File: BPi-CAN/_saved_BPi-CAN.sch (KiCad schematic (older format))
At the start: 82 parts, among them J1 RJ45, J2 RJ45, J3 RJ45, J4 RJ45, P1 BPi, P10 SPI, P11 SNIFFER, P12 CAN-Bus, P13 USB, P14 CAN-Bus, P15 POWER, P16 CAN, P17 CAN, P18 CAN, P19 TERM, P2 S88, P20 S88 CONN, P21 RS232 Con, P22 S88, P3 CONN_02X04, P4 CONN_01X02, P5 TERM, P6 S88, P7 I2C-Bus, P8 RS485, P9 RS232, U1 MCP2562, U10 MCP2562, U11 6N137, U12 ISO1050, U13 FT230XS, U2 LM7805, U3 6N137, U4 6N137, U5 6N137, U6 6N137, U7 ADuM1251BR, U8 MAX3072E, U9 MAX3232

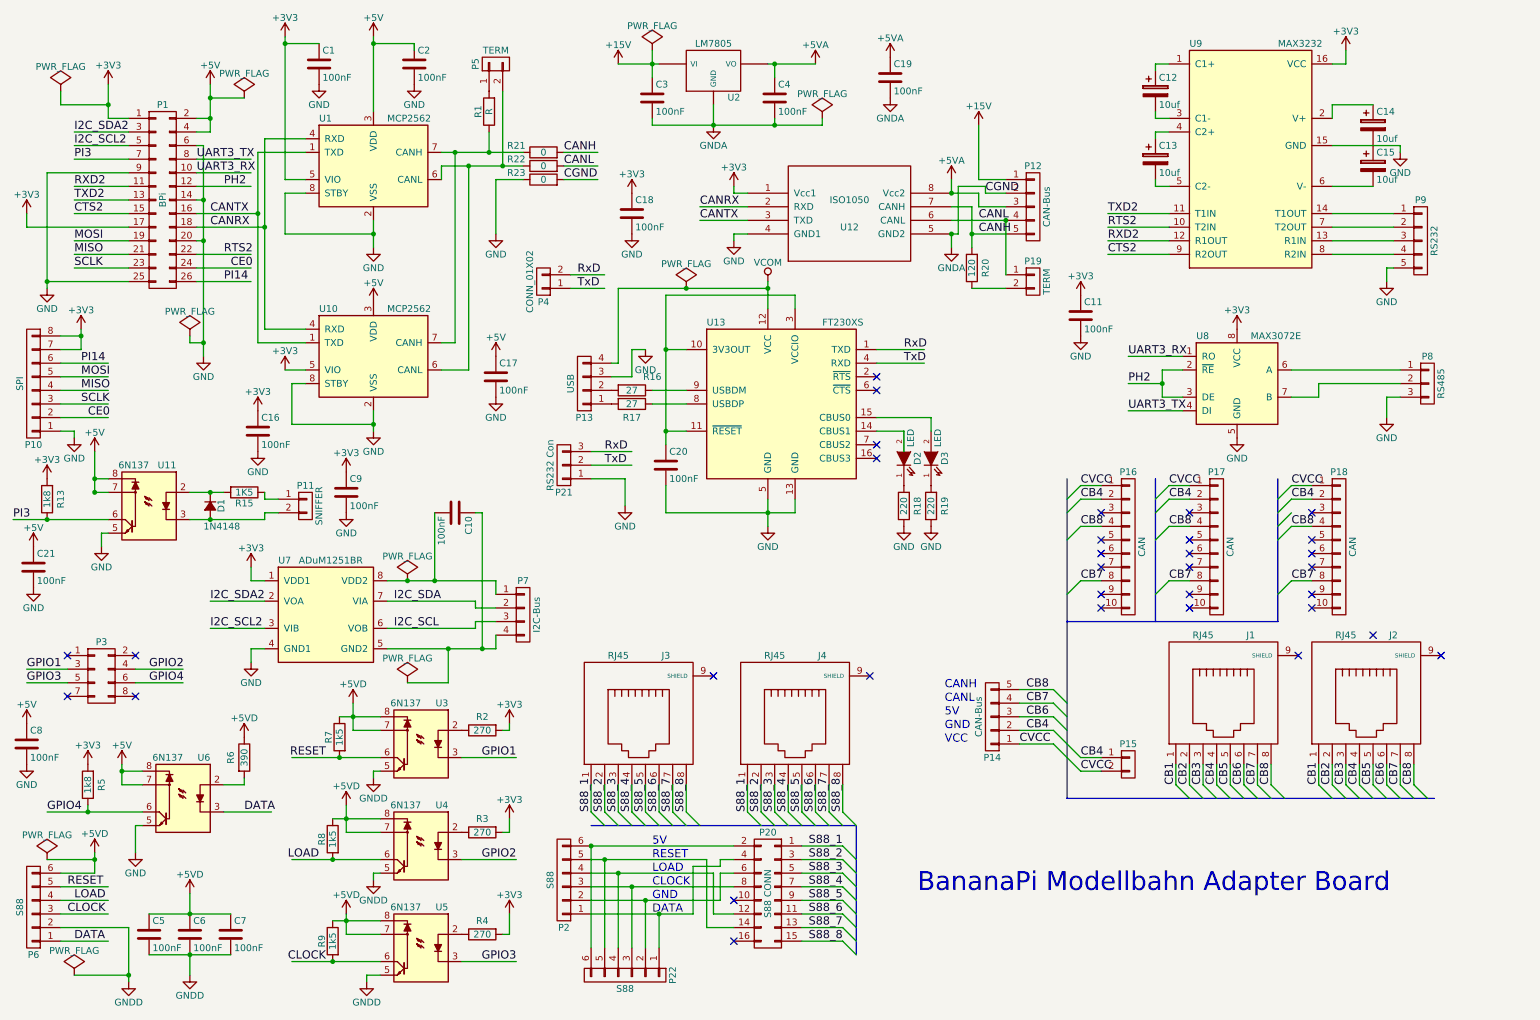
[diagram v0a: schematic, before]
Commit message: add DCDC converter
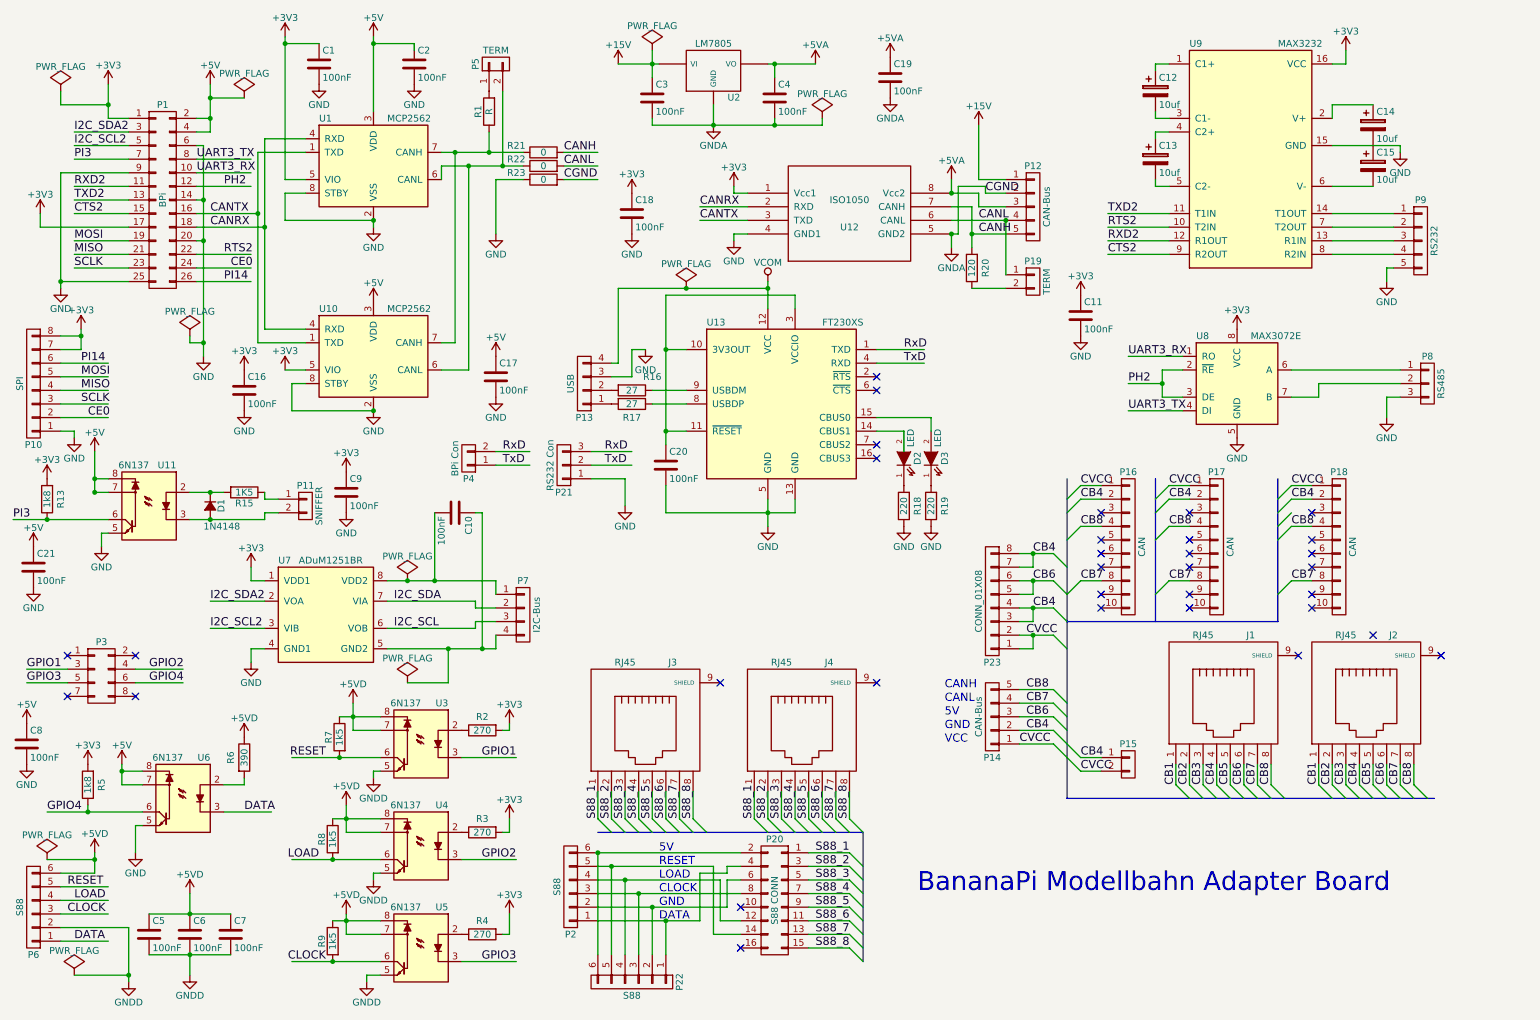
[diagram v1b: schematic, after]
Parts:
- added P23: CONN_01X08, 78xx:DCDC, symbol CONN_01X08
- P4: value CONN_01X02 -> BPi Con
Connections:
- wire segments 350 -> 361
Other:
- moved on the sheet: C16, J3, J4, P2, P20, P22, P4
